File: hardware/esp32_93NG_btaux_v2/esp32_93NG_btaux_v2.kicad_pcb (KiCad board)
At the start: 2 copper layers, 76.2 x 76.2 mm, 50 parts, among them J1 SW_EXT, J2 I2S_MIC, J3 PROG, J4 Conn_01x02_Male, J5 Conn_01x02_Male, J6 Conn_01x02_Male, J7 Conn_01x02_Male, SW2 EN, SW3 BOOT, U1 SN65HVD230, U2 SN65HVD230, U3 PCM5102_Breakout, U4 UDA1334A, U5 SZMMBZ15VALT3G, U6 VXO7805-500-M-TR, U7 NCP1117LPST33T3G, U8 ESP32-MINI-1, U9 SN65HVD230

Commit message: Added top and bottom faceplates. Improved silkscreen labels for pinouts, buttons, connectors.
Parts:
- added H10: MountingHole, kicadlibrary:MountingHole_3.2mm_M3_BARE, F.Cu at (160.8, 105.8)
- added H11: MountingHole, kicadlibrary:MountingHole_3.2mm_M3_BARE, F.Cu at (94.7, 105.8)
- added H12: MountingHole, kicadlibrary:MountingHole_3.2mm_M3_BARE, F.Cu at (94.7, 171.8)
- added H5: MountingHole, kicadlibrary:MountingHole_3.2mm_M3_BARE, F.Cu at (318.3, 171.8)
- added H6: MountingHole, kicadlibrary:MountingHole_3.2mm_M3_BARE, F.Cu at (318.3, 105.8)
- added H7: MountingHole, kicadlibrary:MountingHole_3.2mm_M3_BARE, F.Cu at (252.2, 105.8)
- added H8: MountingHole, kicadlibrary:MountingHole_3.2mm_M3_BARE, F.Cu at (252.2, 171.8)
- added H9: MountingHole, kicadlibrary:MountingHole_3.2mm_M3_BARE, F.Cu at (160.8, 171.8)
- added kibuzzard-62F388AD: G***, kibuzzard-62F388AD, F.Cu at (183.9, 103.3)
- added kibuzzard-62F388AD: G***, kibuzzard-62F388AD, F.Cu at (263.1, 103.3)
- added kibuzzard-62F388E5: G***, kibuzzard-62F388E5, F.Cu at (192.5, 103.3)
- added kibuzzard-62F388E5: G***, kibuzzard-62F388E5, F.Cu at (271.8, 103.3)
- added kibuzzard-62F388ED: G***, kibuzzard-62F388ED, F.Cu at (280.4, 103.3)
- added kibuzzard-62F388ED: G***, kibuzzard-62F388ED, F.Cu at (201.2, 103.3)
- added kibuzzard-62F388F4: G***, kibuzzard-62F388F4, F.Cu at (209.8, 103.3)
- added kibuzzard-62F388F4: G***, kibuzzard-62F388F4, F.Cu at (289.1, 103.3)
- added kibuzzard-62F389F5: G***, kibuzzard-62F389F5, F.Cu at (209.8, 106.8)
- added kibuzzard-62F389F5: G***, kibuzzard-62F389F5, F.Cu at (201.2, 106.8)
- added kibuzzard-62F389F5: G***, kibuzzard-62F389F5, F.Cu at (192.5, 106.8)
- added kibuzzard-62F38A16: G***, kibuzzard-62F38A16, F.Cu at (183.9, 106.8)
- added kibuzzard-62F38AAE: G***, kibuzzard-62F38AAE, F.Cu at (232.6, 173.9)
- added kibuzzard-62F38AAE: G***, kibuzzard-62F38AAE, F.Cu at (242.5, 128.5)
- added kibuzzard-62F38AAE: G***, kibuzzard-62F38AAE, F.Cu at (227.5, 150.7)
- added kibuzzard-62F38AB3: G***, kibuzzard-62F38AB3, F.Cu at (232.3, 171.3)
- added kibuzzard-62F38AB3: G***, kibuzzard-62F38AB3, F.Cu at (232.5, 150.4)
- added kibuzzard-62F38AB3: G***, kibuzzard-62F38AB3, F.Cu at (242.3, 133.6)
- added kibuzzard-62F38AC3: G***, kibuzzard-62F38AC3, F.Cu at (223.8, 173.9)
- added kibuzzard-62F38AEE: G***, kibuzzard-62F38AEE, F.Cu at (223.6, 168.7)
- added kibuzzard-62F38B05: G***, kibuzzard-62F38B05, F.Cu at (232.7, 168.7)
- added kibuzzard-62F38B92: G***, kibuzzard-62F38B92, F.Cu at (178.3, 146.1)
- added kibuzzard-62F38C0E: G***, kibuzzard-62F38C0E, F.Cu at (178.3, 154.6)
- added kibuzzard-62F390B1: G***, kibuzzard-62F390B1, F.Cu at (186.6, 160.5)
- added kibuzzard-62F390B1: G***, kibuzzard-62F390B1, B.Cu at (186.6, 154.7)
- added kibuzzard-62F390B9: G***, kibuzzard-62F390B9, F.Cu at (189.1, 160.6)
- added kibuzzard-62F390B9: G***, kibuzzard-62F390B9, B.Cu at (189.1, 154.6)
- added kibuzzard-62F390E7: G***, kibuzzard-62F390E7, F.Cu at (194.2, 154.7)
- added kibuzzard-62F390E7: G***, kibuzzard-62F390E7, B.Cu at (194.2, 154.2)
- added kibuzzard-62F390F5: G***, kibuzzard-62F390F5, F.Cu at (184.0, 161.1)
- added kibuzzard-62F390F5: G***, kibuzzard-62F390F5, B.Cu at (184.0, 154.1)
- added kibuzzard-62F3919A: G***, kibuzzard-62F3919A, F.Cu at (230.0, 151.5)
- added kibuzzard-62F391F6: G***, kibuzzard-62F391F6, F.Cu at (242.2, 131.1)
- added kibuzzard-62F39221: G***, kibuzzard-62F39221, F.Cu at (235.1, 150.9)
- added kibuzzard-62F39235: G***, kibuzzard-62F39235, F.Cu at (242.6, 141.2)
- added kibuzzard-62F39235: G***, kibuzzard-62F39235, F.Cu at (237.7, 150.8)
- added kibuzzard-62F3924B: G***, kibuzzard-62F3924B, F.Cu at (213.4, 136.2)
- added kibuzzard-62F3924B: G***, kibuzzard-62F3924B, F.Cu at (242.7, 136.2)
- added kibuzzard-62F3924B: G***, kibuzzard-62F3924B, F.Cu at (213.4, 131.1)
- added kibuzzard-62F392E4: G***, kibuzzard-62F392E4, F.Cu at (231.3, 145.2)
- added kibuzzard-62F3934B: G***, kibuzzard-62F3934B, F.Cu at (235.6, 131.2)
- added kibuzzard-62F394C5: G***, kibuzzard-62F394C5, F.Cu at (228.1, 165.6)
- added kibuzzard-62F394F3: G***, kibuzzard-62F394F3, F.Cu at (169.9, 153.8)
- added kibuzzard-62F39580: G***, kibuzzard-62F39580, F.Cu at (169.9, 148.3)
- added kibuzzard-62F39586: G***, kibuzzard-62F39586, F.Cu at (180.8, 146.4)
- added kibuzzard-62F395A5: G***, kibuzzard-62F395A5, F.Cu at (217.4, 157.6)
- added mouse-bite-2.54mm-slot: VAL**, kicadlibrary:mouse-bite-2.54mm-slot, F.Cu at (167.1, 167.1)
- added mouse-bite-2.54mm-slot: VAL**, kicadlibrary:mouse-bite-2.54mm-slot, F.Cu at (245.9, 167.1)
- added mouse-bite-2.54mm-slot: VAL**, kicadlibrary:mouse-bite-2.54mm-slot, F.Cu at (167.1, 153.2)
- added mouse-bite-2.54mm-slot: VAL**, kicadlibrary:mouse-bite-2.54mm-slot, F.Cu at (167.1, 111.3)
- added mouse-bite-2.54mm-slot: VAL**, kicadlibrary:mouse-bite-2.54mm-slot, F.Cu at (245.9, 139.2)
- added mouse-bite-2.54mm-slot: VAL**, kicadlibrary:mouse-bite-2.54mm-slot, F.Cu at (167.1, 125.2)
- added mouse-bite-2.54mm-slot: VAL**, kicadlibrary:mouse-bite-2.54mm-slot, F.Cu at (167.1, 139.2)
- added mouse-bite-2.54mm-slot: VAL**, kicadlibrary:mouse-bite-2.54mm-slot, F.Cu at (245.9, 125.2)
- added mouse-bite-2.54mm-slot: VAL**, kicadlibrary:mouse-bite-2.54mm-slot, F.Cu at (245.9, 111.3)
- moved SW2 79.4 mm to (173.4, 153.9)
- moved C11 75.4 mm to (184.3, 140.6)
- moved R10 75.4 mm to (189.7, 135.9)
- moved C1 75.4 mm to (171.8, 115.8)
- moved C10 75.4 mm to (209.3, 151.0)
- moved C12 75.4 mm to (218.2, 165.5)
- moved C2 75.4 mm to (176.8, 117.2)
- moved C3 75.4 mm to (171.8, 113.7)
- moved C4 75.4 mm to (189.1, 130.6)
- moved C5 75.4 mm to (184.3, 136.8)
- moved C6 75.4 mm to (182.0, 140.6)
- moved C7 75.4 mm to (215.8, 165.5)
- moved C8 75.4 mm to (202.7, 151.0)
- moved C9 75.4 mm to (182.0, 136.8)
- moved J2 75.4 mm to (226.8, 168.7)
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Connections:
- J5 pad 1: CAN_L -> CAN_H
- J5 pad 2: CAN_H -> CAN_L
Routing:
- net CAN_H: track 27.1 -> 31.4 mm
- net I2S0_BCK: track 41.8 -> 45.3 mm
- net I2S0_WSEL: track 39.8 -> 43.3 mm
- net I2S0_DOUT: track 40.6 -> 44.0 mm
- net CAN_L: track 30.5 -> 29.1 mm
- net HPD_OUT_L: track 27.3 -> 26.8 mm
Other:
- board size 76.2 x 76.2 mm -> 233.7 x 76.2 mm
- board text removed: "0"
- board text removed: "0 mm"
- board text removed: "0.01 mm"
- board text removed: "0.02"
- board text removed: "0.035 mm"
- board text removed: "1"
- board text removed: "1.51 mm"
- board text removed: "3.3"
- board text removed: "4.5"
- board text removed: "B.Cu"
- board text removed: "B.Mask"
- board text removed: "B.Paste"
- board text removed: "B.Silkscreen"
- board text removed: "Bottom Silk Screen"
- board text removed: "Bottom Solder Mask"
- board text removed: "Bottom Solder Paste"
- board text removed: "Color"
- board text removed: "Dielectric"
- board text removed: "Epsilon R"
- board text removed: "F.Cu"
- board text removed: "F.Mask"
- board text removed: "F.Paste"
- board text removed: "F.Silkscreen"
- board text removed: "FR4"
- board text removed: "Layer Name"
- board text removed: "Loss Tangent"
- board text removed: "Material"
- board text removed: "Not specified"
- board text removed: "PCM5102"
- board text removed: "Thickness (mm)"
- board text removed: "Top Silk Screen"
- board text removed: "Top Solder Mask"
- board text removed: "Top Solder Paste"
- board text removed: "Type"
- board text removed: "UDA1334H"
- board text removed: "copper"
- board text removed: "core"

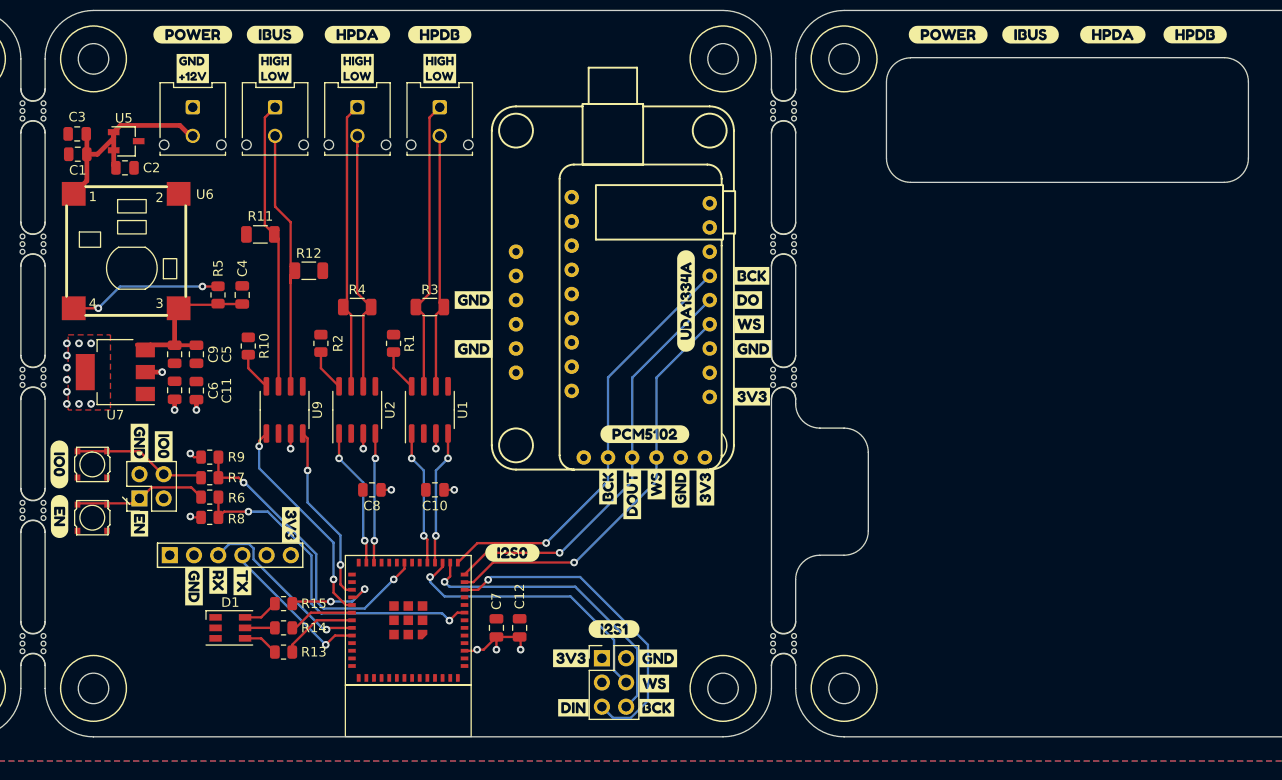
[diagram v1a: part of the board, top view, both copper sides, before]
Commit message: Adjusted silkscreen labels to reduce clutter. Added GPIO header for external buttons or LEDs. Added second PCB faceplate, for the bottom-side of the assembly.
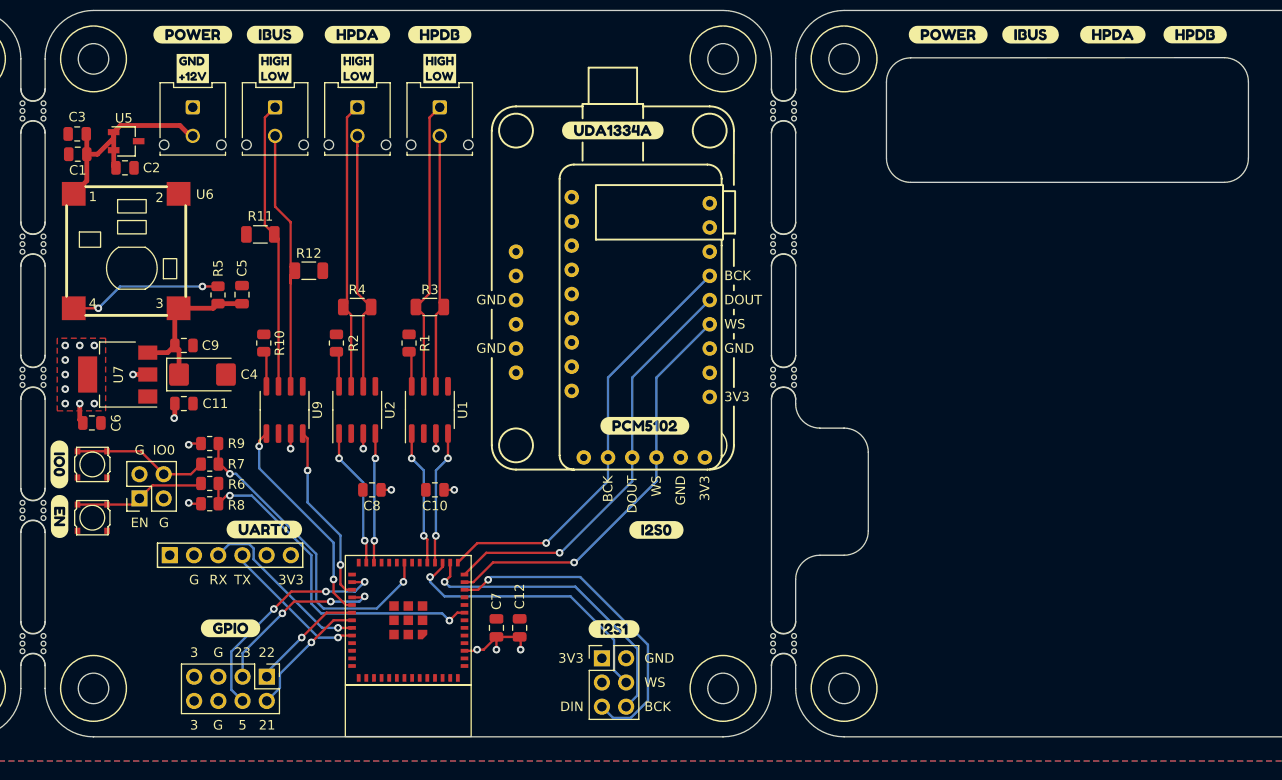
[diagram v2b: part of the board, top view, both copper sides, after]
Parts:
- removed D1: LED_RGB, LED_SMD:LED_RGB_PLCC-6
- removed R13, R14, R15: 1K, Resistor_SMD:R_0805_2012Metric
- removed kibuzzard-62F38AAE (x3): G***, kibuzzard-62F38AAE
- removed kibuzzard-62F38AB3 (x3): G***, kibuzzard-62F38AB3
- removed kibuzzard-62F38AC3: G***, kibuzzard-62F38AC3
- removed kibuzzard-62F38AEE: G***, kibuzzard-62F38AEE
- removed kibuzzard-62F38B05: G***, kibuzzard-62F38B05
- removed kibuzzard-62F38B92: G***, kibuzzard-62F38B92
- removed kibuzzard-62F38C0E: G***, kibuzzard-62F38C0E
- removed the kibuzzard-62F390B1 at (186.6, 160.5)
- removed the kibuzzard-62F390B9 at (189.1, 160.6)
- removed the kibuzzard-62F390E7 at (194.2, 154.7)
- removed the kibuzzard-62F390F5 at (184.0, 161.1)
- removed kibuzzard-62F3919A: G***, kibuzzard-62F3919A
- removed kibuzzard-62F391F6: G***, kibuzzard-62F391F6
- removed kibuzzard-62F39221: G***, kibuzzard-62F39221
- removed kibuzzard-62F39235 (x2): G***, kibuzzard-62F39235
- removed kibuzzard-62F3924B (x3): G***, kibuzzard-62F3924B
- removed kibuzzard-62F39586: G***, kibuzzard-62F39586
- added J8: Conn_GPIO, Connector_PinHeader_2.54mm:PinHeader_2x04_P2.54mm_Vertical, F.Cu at (191.7, 170.6)
- added kibuzzard-62F44F39: G***, kibuzzard-62F44F39, F.Cu at (187.9, 165.5)
- added kibuzzard-62F4510B: G***, kibuzzard-62F4510B, F.Cu at (191.4, 155.2)
- C4: footprint Capacitor_SMD:C_0805_2012Metric -> Capacitor_Tantalum_SMD:CP_EIA-6032-20_AVX-F
- J4: value Conn_01x02_Male -> Conn_VCC
- J5: value Conn_01x02_Male -> Conn_CAN_IBUS
- J6: value Conn_01x02_Male -> Conn_HPD_IN
- J7: value Conn_01x02_Male -> Conn_HPD_Out
- moved kibuzzard-62F3934B 19.5 mm to (228.0, 113.3), turned to 0 degrees
- moved kibuzzard-62F395A5 15.3 mm to (232.5, 155.2)
- moved C6 9.33 mm to (173.3, 144.0), turned to 0 degrees
- moved C4 9.33 mm to (184.9, 138.9), turned to 0 degrees
- moved C5 7.87 mm to (189.1, 130.5), turned to 90 degrees
- moved C11 1.89 mm to (183.0, 142.0), turned to 0 degrees
- moved R10 1.66 mm to (191.3, 135.6)
- moved R2 1.63 mm to (199.0, 135.6)
- moved R1 1.63 mm to (206.6, 135.6)
- moved R6 1.43 mm to (185.7, 150.3)
- moved R8 1.43 mm to (185.7, 152.5)
- moved R9 1.43 mm to (185.7, 146.1)
- moved R7 1.43 mm to (185.7, 148.3)
- moved C9 1.34 mm to (183.0, 135.9), turned to 0 degrees
- moved kibuzzard-62F392E4 0.87 mm to (231.3, 144.3)
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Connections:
- U8 pad 29: unconnected-(U8-Pad29) -> /ESP32/IO5
- U8 pad 31: Net-(R15-Pad1) -> /ESP32/IO23
- U8 pad 33: Net-(R14-Pad1) -> /ESP32/IO22
- U8 pad 34: Net-(R13-Pad1) -> /ESP32/IO21
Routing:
- net /ESP32/IO5: track 0.00 -> 24.0 mm, vias 0 -> 3
- net /ESP32/IO23: track 0.00 -> 19.1 mm, vias 0 -> 3
- net /ESP32/IO21: track 0.00 -> 13.3 mm, vias 0 -> 1
- net /ESP32/IO22: track 0.00 -> 12.0 mm, vias 0 -> 1
- net Net-(R15-Pad1): track 9.92 -> 0.00 mm, vias 2 -> 0
- net Net-(R13-Pad1): track 8.10 -> 0.00 mm
- net Net-(R14-Pad1): track 6.93 -> 0.00 mm
- net Net-(D1-Pad6): track 3.72 -> 0.00 mm
- net Net-(D1-Pad4): track 3.72 -> 0.00 mm
- net Net-(D1-Pad5): track 3.13 -> 0.00 mm
- net +3V3: track 22.8 -> 24.3 mm, vias 23 -> 21
- net IO0: track 32.6 -> 34.0 mm
- net CAN_H: track 31.4 -> 30.3 mm
- net Net-(R2-Pad1): track 4.39 -> 3.75 mm
- net Net-(R1-Pad1): track 4.39 -> 3.75 mm
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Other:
- board text added: "21"
- board text added: "22"
- board text added: "23"
- board text added: "3"
- board text added: "3V3"
- board text added: "5"
- board text added: "BCK"
- board text added: "DIN"
- board text added: "DOUT"
- board text added: "EN"
- board text added: "G"
- board text added: "GND"
- board text added: "IO0"
- board text added: "RX"
- board text added: "TX"
- board text added: "WS"

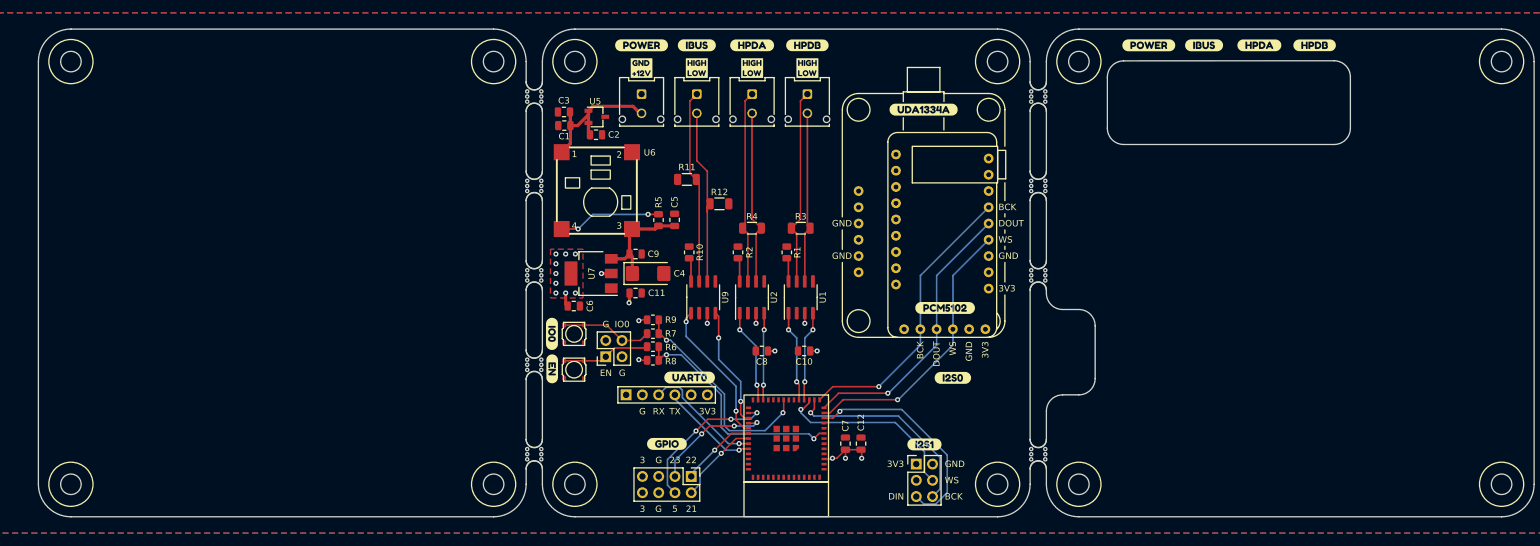
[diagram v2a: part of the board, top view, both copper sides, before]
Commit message: Updated silkscreen
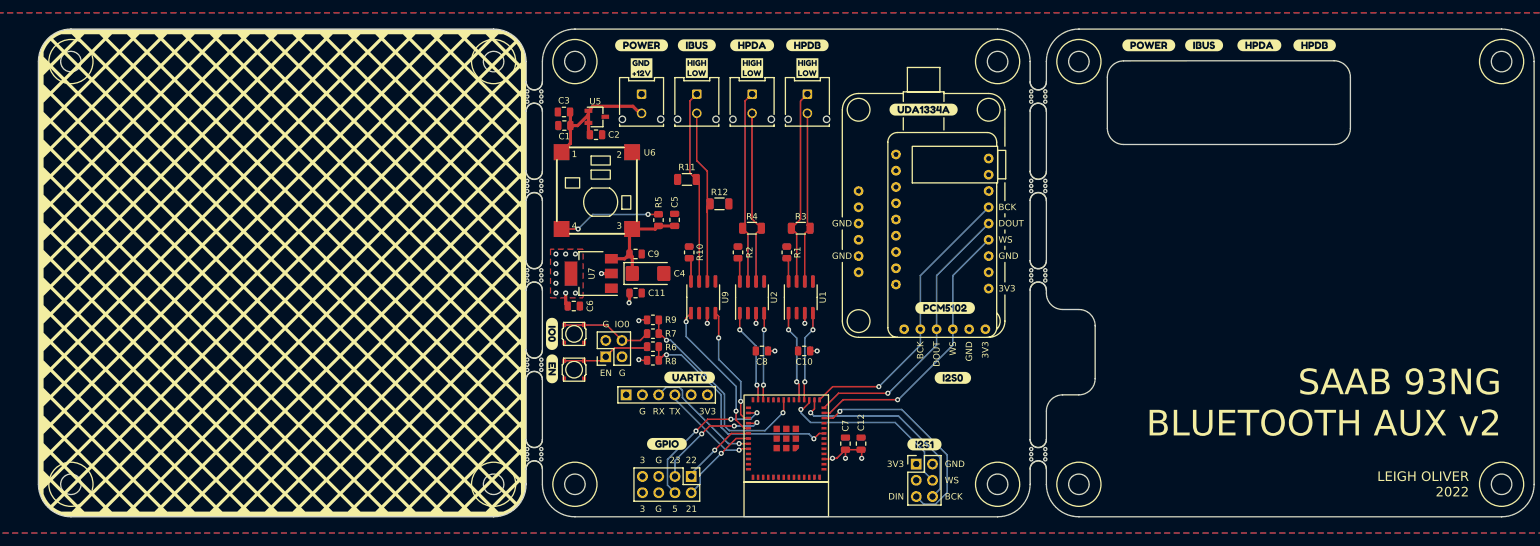
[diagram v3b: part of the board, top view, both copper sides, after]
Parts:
- removed kibuzzard-62F390B1: G***, kibuzzard-62F390B1
- removed kibuzzard-62F390B9: G***, kibuzzard-62F390B9
- removed kibuzzard-62F390E7: G***, kibuzzard-62F390E7
- removed kibuzzard-62F390F5: G***, kibuzzard-62F390F5
- added kibuzzard-62F394C5: G***, kibuzzard-62F394C5, B.Cu at (228.1, 165.6)
- added kibuzzard-62F44F39: G***, kibuzzard-62F44F39, B.Cu at (187.8, 175.4)
- added kibuzzard-62F4510B: G***, kibuzzard-62F4510B, B.Cu at (191.8, 153.3)
- added kibuzzard-62F9EF46: G***, kibuzzard-62F9EF46, B.Cu at (179.6, 146.8)
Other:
- board text added: "LEIGH OLIVER 2022"
- board text added: "SAAB 93NG BLUETOOTH AUX v2"

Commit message: Started working on module-based V2 PCB, which is easier to build.
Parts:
- removed H10, H11, H12, H5, H6, H7, H8, H9: MountingHole, kicadlibrary:MountingHole_3.2mm_M3_BARE
- removed J3: PROG, Connector_PinHeader_2.54mm:PinHeader_1x06_P2.54mm_Horizontal
- removed J6: Conn_HPD_IN, kicadlibrary:Molex_Micro-Fit_3.0_43045-0212_2x01_P3.00mm_Vertical
- removed J7: Conn_HPD_Out, kicadlibrary:Molex_Micro-Fit_3.0_43045-0212_2x01_P3.00mm_Vertical
- removed J8: Conn_GPIO, Connector_PinHeader_2.54mm:PinHeader_2x04_P2.54mm_Vertical
- removed R1, R2: 100K, Resistor_SMD:R_0805_2012Metric
- removed R3, R4: 120, Resistor_SMD:R_1206_3216Metric
- removed SW2: EN, kicadlibrary:R-667834
- removed SW3: BOOT, kicadlibrary:R-667834
- removed U1, U2: SN65HVD230, Package_SO:SOIC-8_3.9x4.9mm_P1.27mm
- removed kibuzzard-62F388AD (x2): G***, kibuzzard-62F388AD
- removed kibuzzard-62F388E5 (x2): G***, kibuzzard-62F388E5
- removed kibuzzard-62F388ED (x2): G***, kibuzzard-62F388ED
- removed kibuzzard-62F388F4 (x2): G***, kibuzzard-62F388F4
- removed kibuzzard-62F389F5 (x3): G***, kibuzzard-62F389F5
- removed kibuzzard-62F38A16: G***, kibuzzard-62F38A16
- removed kibuzzard-62F394F3: G***, kibuzzard-62F394F3
- removed kibuzzard-62F39580: G***, kibuzzard-62F39580
- removed kibuzzard-62F44F39 (x2): G***, kibuzzard-62F44F39
- removed kibuzzard-62F4510B (x2): G***, kibuzzard-62F4510B
- removed kibuzzard-62F9EF46: G***, kibuzzard-62F9EF46
- removed mouse-bite-2.54mm-slot (x9): VAL**, kicadlibrary:mouse-bite-2.54mm-slot
- J4, J5: footprint kicadlibrary:Molex_Micro-Fit_3.0_43045-0212_2x01_P3.00mm_Vertical -> kicadlibrary:Molex_Mega-Fit_76825-0002_2x01_P5.70mm_Horizontal
- moved H1 99.1 mm to (338.6, 171.8)
- moved H2 99.1 mm to (338.6, 105.8)
- moved H3 99.1 mm to (272.5, 105.8)
- moved H4 99.1 mm to (272.5, 171.8)
- moved C7 63.0 mm to (154.1, 152.5)
- moved kibuzzard-62F394C5 61.1 mm to (167.1, 161.0), turned to 90 degrees
- moved kibuzzard-62F394C5 61.1 mm to (167.1, 161.0), turned to -90 degrees
- moved C12 59.8 mm to (159.8, 152.5)
- moved J2 57.0 mm to (170.2, 162.3), turned to 90 degrees
- moved kibuzzard-62F395A5 49.0 mm to (183.9, 161.2), turned to -90 degrees
- moved kibuzzard-62F3934B 43.3 mm to (225.8, 156.6), turned to -90 degrees
- moved kibuzzard-62F392E4 39.7 mm to (194.8, 160.0), turned to -90 degrees
- moved U8 36.2 mm to (176.0, 145.2), turned to 90 degrees
- moved J4 34.3 mm to (216.2, 122.3), turned to -90 degrees
- moved U3 32.1 mm to (190.3, 151.0), turned to 0 degrees
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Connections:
- U8 pad 17: HPD_OUT_RX -> IO12
- U8 pad 18: HPD_OUT_TX -> IO13
- U8 pad 25: HPD_IN_RX -> IO9
- U8 pad 26: HPD_IN_TX -> IO10
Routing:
- net I2S0_BCK: track 45.2 -> 0.00 mm, vias 1 -> 0
- net I2S0_DOUT: track 44.0 -> 0.00 mm, vias 1 -> 0
- net I2S0_WSEL: track 43.3 -> 0.00 mm, vias 1 -> 0
- net EN: track 37.0 -> 0.00 mm, vias 2 -> 0
- net I2S1_DIN: track 34.7 -> 0.00 mm, vias 1 -> 0
- net IO0: track 34.0 -> 0.00 mm, vias 2 -> 0
- net I2S1_BCK: track 32.0 -> 0.00 mm, vias 1 -> 0
- net HPD_OUT_H: track 30.7 -> 0.00 mm
- net CAN_H: track 30.3 -> 0.00 mm
- net HPD_IN_H: track 30.2 -> 0.00 mm
- net I2S1_WSEL: track 29.5 -> 0.00 mm, vias 1 -> 0
- net CAN_L: track 29.1 -> 0.00 mm
- net HPD_IN_L: track 28.4 -> 0.00 mm
- net HPD_OUT_L: track 26.8 -> 0.00 mm
- net +3V3: track 24.3 -> 0.00 mm, vias 21 -> 0
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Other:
- board outline removed
- board text removed: "21"
- board text removed: "22"
- board text removed: "23"
- board text removed: "3"
- board text removed: "5"
- board text removed: "CP2102 BREAKOUT"
- board text removed: "EN"
- board text removed: "G"
- board text removed: "IO0"
- board text removed: "LEIGH OLIVER 2022"
- board text removed: "RX"
- board text removed: "SAAB 93NG BLUETOOTH AUX v2"
- board text removed: "TODO ADD ANOTHER COVER LAYER SPECIAL STANDOFFS FOR THREE LAYER STACKUP? https://www.digikey.com.au/en/products/detail/keystone-electronics/24882/9921822"
- board text removed: "TX"
